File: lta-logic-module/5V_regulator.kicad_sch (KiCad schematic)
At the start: 8 parts

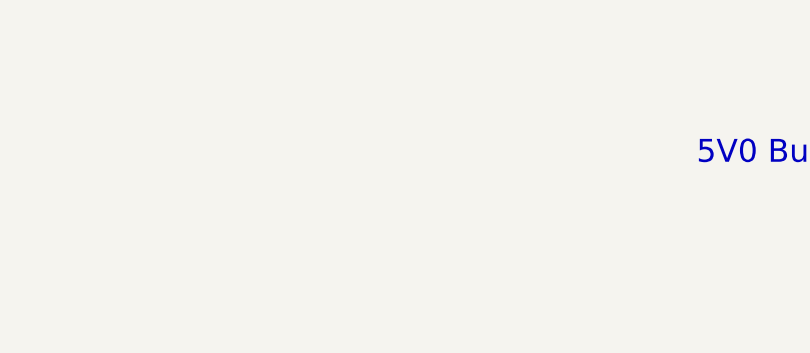
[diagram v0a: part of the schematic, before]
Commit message: Add test points
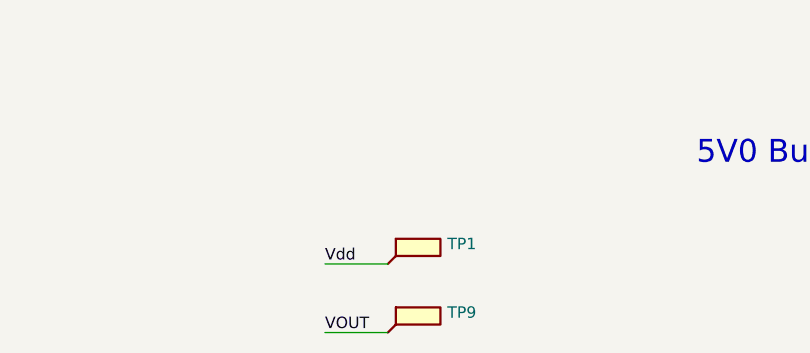
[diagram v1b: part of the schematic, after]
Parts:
- added TP1, TP9: (no value), symbol Connector:TestPoint_Flag
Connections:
- net VOUT: now also TP9.1
- net Vdd: now also TP1.1
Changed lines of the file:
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@@
+    (stroke (width 0) (type default) (color 0 0 0 0))
+  )
+  (wire (pts (xy 146.05 185.42) (xy 153.035 185.42))
     (stroke (width 0) (type default) (color 0 0 0 0))
   )
@@
   )
   (wire (pts (xy 22.86 33.655) (xy 28.575 33.655))
+    (stroke (width 0) (type default) (color 0 0 0 0))
+  )
+  (wire (pts (xy 146.05 193.04) (xy 153.035 193.04))
     (stroke (width 0) (type default) (color 0 0 0 0))
   )
@@
     (effects (font (size 1.27 1.27)) (justify left bottom))
   )
+  (label "VOUT" (at 146.05 193.04 0)
+    (effects (font (size 1.27 1.27)) (justify left bottom))
+  )
   (label "VBATT" (at 89.535 64.77 0)
     (effects (font (size 1.27 1.27)) (justify left bottom))
@@
   )
   (label "Vdd" (at 161.29 69.85 0)
+    (effects (font (size 1.27 1.27)) (justify left bottom))
+  )
+  (label "Vdd" (at 146.05 185.42 0)
     (effects (font (size 1.27 1.27)) (justify left bottom))
   )
@@
     (pin "1")
   )
+  (symbol (lib_id "Connector:TestPoint_Flag") (at 153.035 193.04 0) (unit 1)
+    (in_bom no) (on_board yes) (fields_autoplaced)
+    (property "Reference" "TP9" (id 0) (at 159.639 190.8083 0)
+      (effects (font (size 1.27 1.27)) (justify left))
+    )
+    (property "Value" "" (id 1) (at 159.639 193.3452 0)
+      (effects (font (size 1.27 1.27)) (justify left))
+    )
+    (property "Footprint" "" (id 2) (at 158.115 193.04 0)
+      (effects (font (size 1.27 1.27)) hide)
+    )
+    (property "Datasheet" "~" (id 3) (at 158.115 193.04 0)
+      (effects (font (size 1.27 1.27)) hide)
+    )
+    (pin "1")
+  )
   (symbol (lib_id "power:GND") (at 107.315 79.375 0) (unit 1)
     (in_bom yes) (on_board yes)
@@
       (effects (font (size 1.27 1.27)) hide)
     )
+    (pin "1")
+  )
+  (symbol (lib_id "Connector:TestPoint_Flag") (at 153.035 185.42 0) (unit 1)
+    (in_bom no) (on_board yes) (fields_autoplaced)
+    (property "Reference" "TP1" (id 0) (at 159.639 183.1883 0)
+      (effects (font (size 1.27 1.27)) (justify left))
+    )
+    (property "Value" "" (id 1) (at 159.639 185.7252 0)
+      (effects (font (size 1.27 1.27)) (justify left))
+    )
+    (property "Footprint" "" (id 2) (at 158.115 185.42 0)
+      (effects (font (size 1.27 1.27)) hide)
+    )
+    (property "Datasheet" "~" (id 3) (at 158.115 185.42 0)
+      (effects (font (size 1.27 1.27)) hide)
+    )

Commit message: Fix GND path return.
* Route power traces over ground plane.
* Add routed corners to edge cuts
* Remove final TODO notes.
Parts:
- C5: Comment 220u 35V low-ESR (<=160mOhm), I_RMS>250mA aluminum -> 220u 20% 35V low-ESR (<=160mOhm), I_RMS>250mA aluminum
- C6: Comment 68u AVX TPS 20V low-ESR (<=150mOhm) solid tantalum; exact M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 -> 68u 10% AVX TPS 20V low-ESR (<=150mOhm) solid tantalum; exa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
- D3: Comment Vf=2.0V 20mA test current red LED -> Vf=2.0V I_test=20mA red LED
- L1: Comment Exact MFR/MPN required -> 150uH, Exact MFR/MPN required
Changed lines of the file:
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@@
       (effects (font (size 1.27 1.27)) hide)
     )
-    (property "Comment" "220u 35V low-ESR (<=160mOhm), I_RMS>250mA aluminum" (id 4) (at 96.52 70.485 0)
+    (property "Comment" "220u 20% 35V low-ESR (<=160mOhm), I_RMS>250mA aluminum" (id 4) (at 96.52 70.485 0)
       (effects (font (size 1.27 1.27)) hide)
     )
@@
       (effects (font (size 1.27 1.27)) hide)
     )
-    (property "Comment" "Exact MFR/MPN required" (id 6) (at 148.59 69.85 0)
+    (property "Comment" "150uH, Exact MFR/MPN required" (id 6) (at 148.59 69.85 0)
       (effects (font (size 1.27 1.27)) hide)
     )
@@
       (effects (font (size 1.27 1.27)) hide)
     )
-    (property "Comment" "68u AVX TPS 20V low-ESR (<=150mOhm) solid tantalum; exact MPN" (id 4) (at 154.305 77.47 0)
+    (property "Comment" "68u 10% AVX TPS 20V low-ESR (<=150mOhm) solid tantalum; exact MPN" (id 4) (at 154.305 77.47 0)
       (effects (font (size 1.27 1.27)) hide)
     )
@@
       (effects (font (size 1.27 1.27)) hide)
     )
-    (property "Comment" "Vf=2.0V 20mA test current red LED" (id 6) (at 176.53 109.22 90)
-      (effects (font (size 1.27 1.27)) hide)
-    )
+    (property "Comment" "Vf=2.0V I_test=20mA red LED" (id 6) (at 176.53 109.22 90)
+      (effects (font (size 1.27 1.27)) hide)
+    )

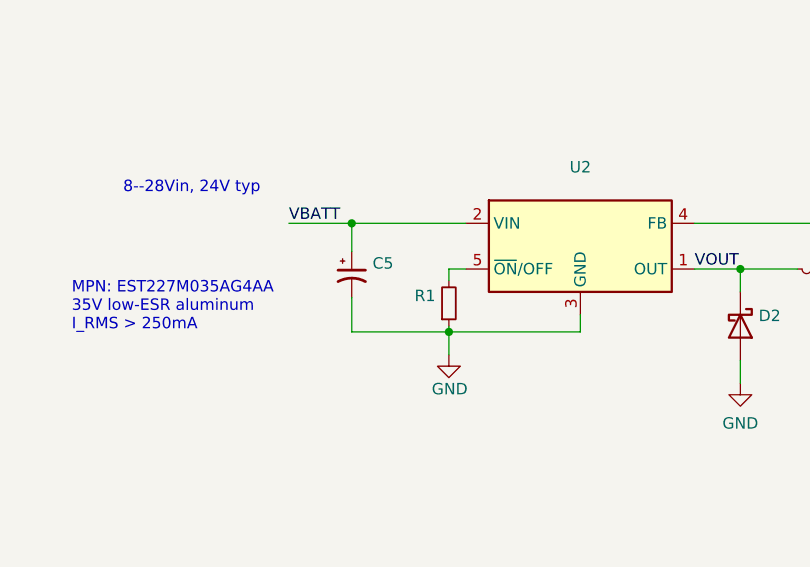
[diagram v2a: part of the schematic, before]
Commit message: Add indicator LED to SW1 enabled.
Adds 220K pull-down resistor to DARK signal. (Validated.)
Update solder thief pads and process direction indicator.
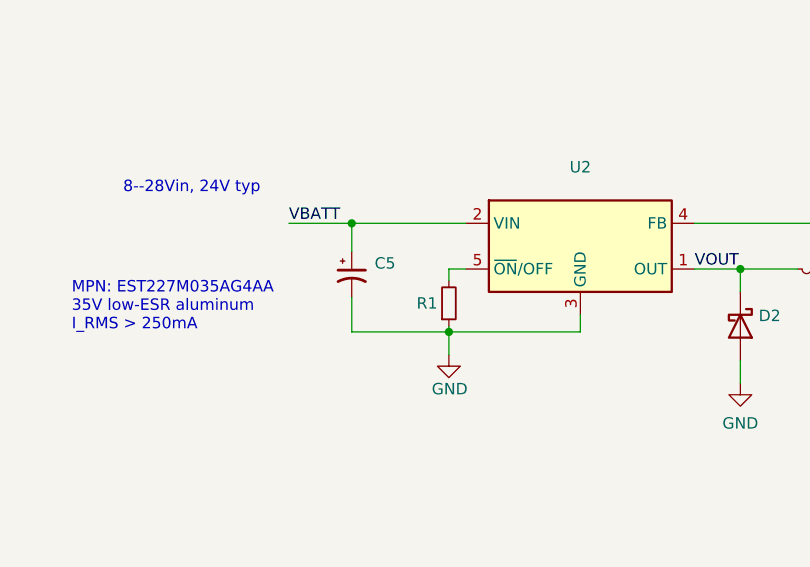
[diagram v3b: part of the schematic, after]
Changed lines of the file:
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@@
   )
   (symbol (lib_id "Device:R_Small") (at 107.315 73.66 0) (mirror x) (unit 1)
-    (in_bom yes) (on_board yes) (fields_autoplaced)
-    (property "Reference" "R1" (id 0) (at 105.8165 72.8253 0)
+    (in_bom yes) (on_board yes)
+    (property "Reference" "R1" (id 0) (at 106.045 73.66 0)
       (effects (font (size 1.27 1.27)) (justify right))
     )
-    (property "Value" "" (id 1) (at 105.8165 75.3622 0)
+    (property "Value" "" (id 1) (at 106.045 75.565 0)
       (effects (font (size 1.27 1.27)) (justify right))
     )
@@
   )
   (symbol (lib_id "Device:C_Polarized_Small_US") (at 96.52 70.485 0) (unit 1)
-    (in_bom yes) (on_board yes) (fields_autoplaced)
-    (property "Reference" "C5" (id 0) (at 98.8314 69.2185 0)
+    (in_bom yes) (on_board yes)
+    (property "Reference" "C5" (id 0) (at 99.06 69.215 0)
       (effects (font (size 1.27 1.27)) (justify left))
     )
-    (property "Value" "" (id 1) (at 98.8314 71.7554 0)
+    (property "Value" "" (id 1) (at 98.425 71.12 0)
       (effects (font (size 1.27 1.27)) (justify left))
     )

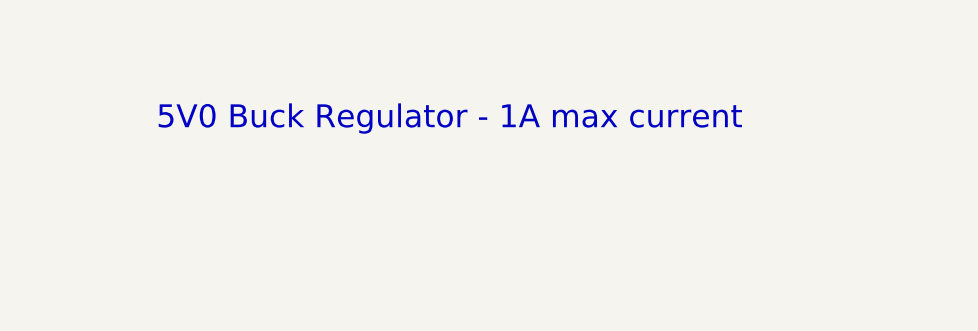
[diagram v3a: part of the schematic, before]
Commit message: Generate logic module 2022-05-08 v1.0 fab documentation.
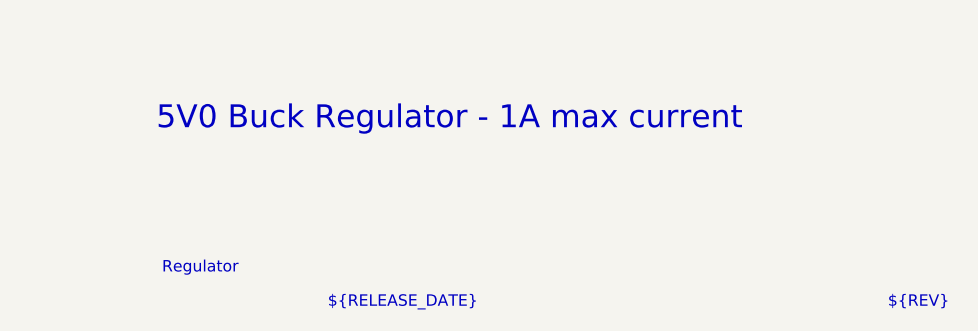
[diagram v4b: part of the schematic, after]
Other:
- note added: "${RELEASE_DATE}"
- note added: "${REV}"
- note added: "Regulator"
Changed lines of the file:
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@@
     (stroke (width 0) (type default) (color 0 0 0 0))
+  )
+  (text "Regulator" (at 187.96 190.5 0)
+    (effects (font (size 1.27 1.27)) (justify left bottom))
   )
   (text "MPN: EST227M035AG4AA\n35V low-ESR aluminum\nI_RMS > 250mA\n"
@@
     (effects (font (size 1.27 1.27)) (justify left bottom))
   )
+  (text "${RELEASE_DATE}" (at 206.375 194.31 0)
+    (effects (font (size 1.27 1.27)) (justify left bottom))
+  )
+  (text "${REV}" (at 268.605 194.31 0)
+    (effects (font (size 1.27 1.27)) (justify left bottom))
+  )
